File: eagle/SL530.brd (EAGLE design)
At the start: 100 x 100 mm, 42 parts, among them IC4 74LVC1G17DBV, IC5 74LVC1G17DBV, U1 LM1117, X1 MC68000

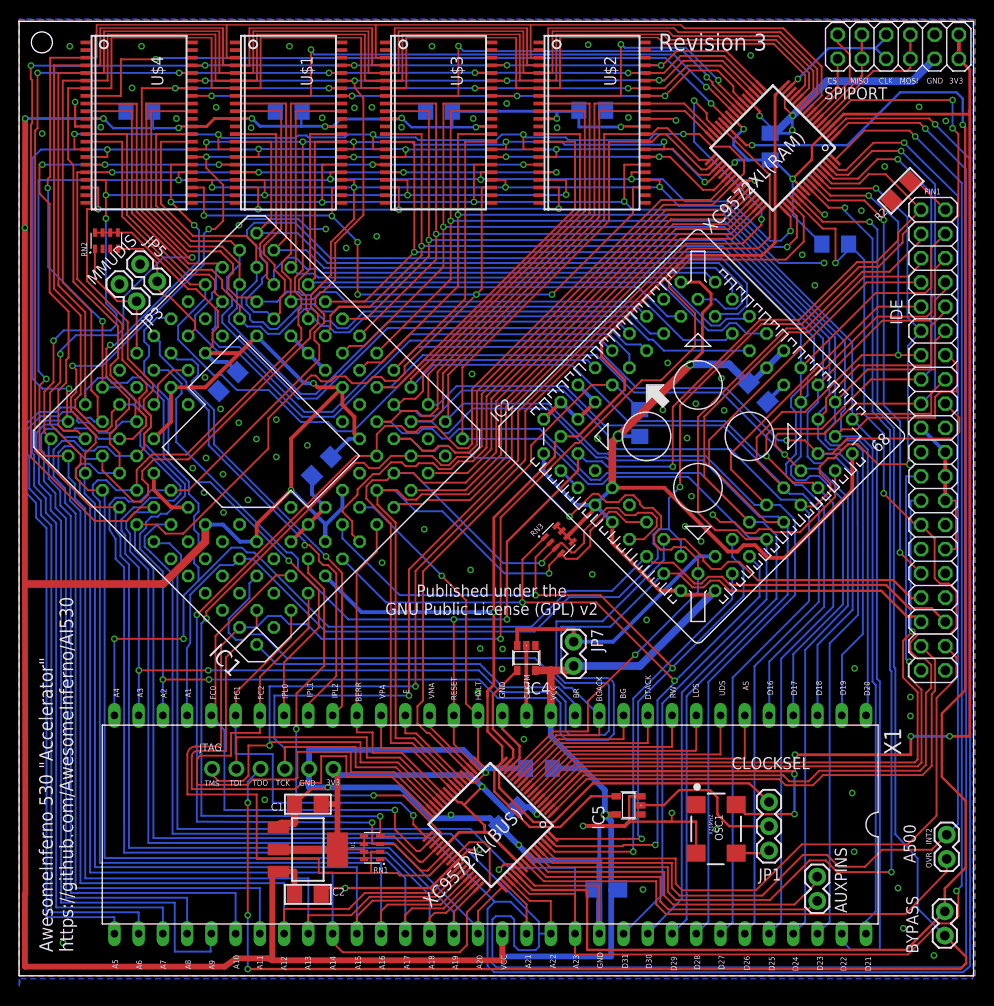
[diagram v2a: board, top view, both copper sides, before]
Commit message: Added solder thieves
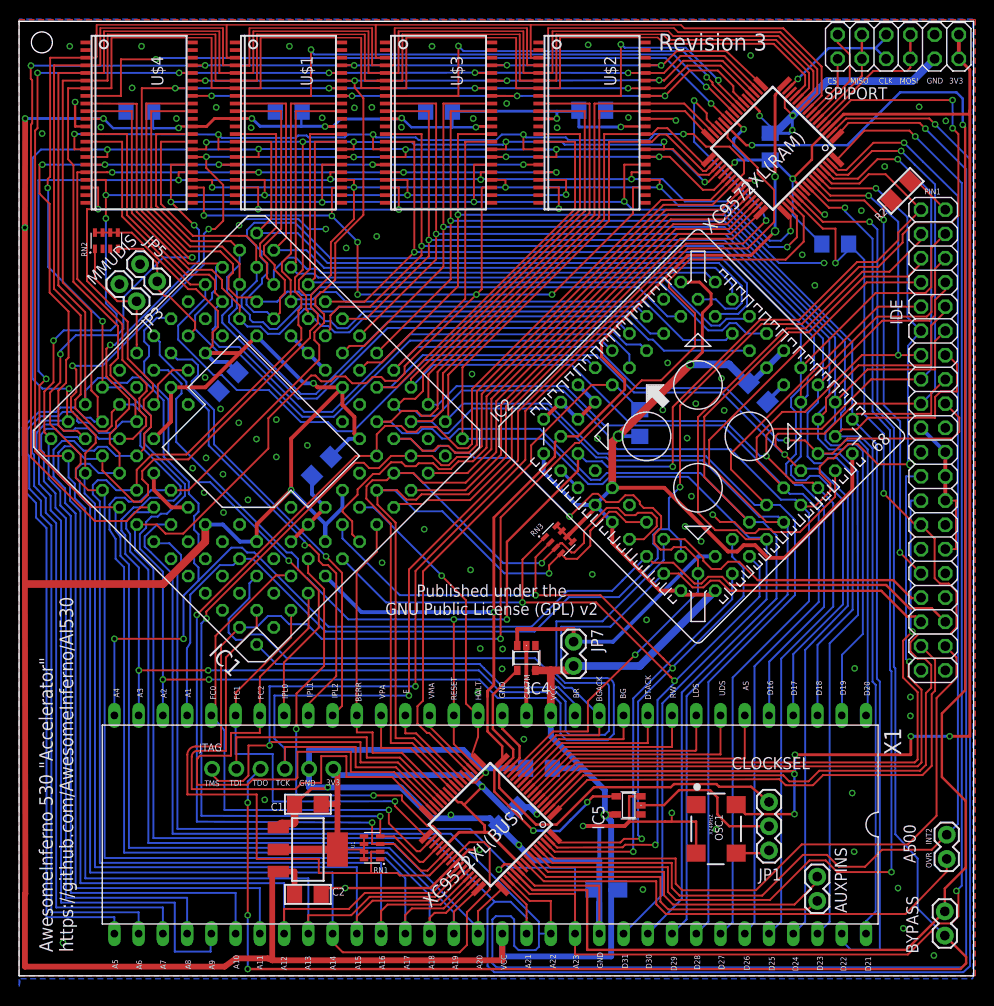
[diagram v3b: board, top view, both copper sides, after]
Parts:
- OSC1: value X20MHZ -> X24MHZ
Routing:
- net FC1: track 44.8 -> 44.3 mm
- net CLKCPU: track 130.3 -> 130.1 mm, vias 1 -> 5
